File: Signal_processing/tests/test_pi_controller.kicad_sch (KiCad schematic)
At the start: 4 parts, among them X1 Integrator, x1 2nd_Order_Transfer_Function, x2 1st Order Transfer Function

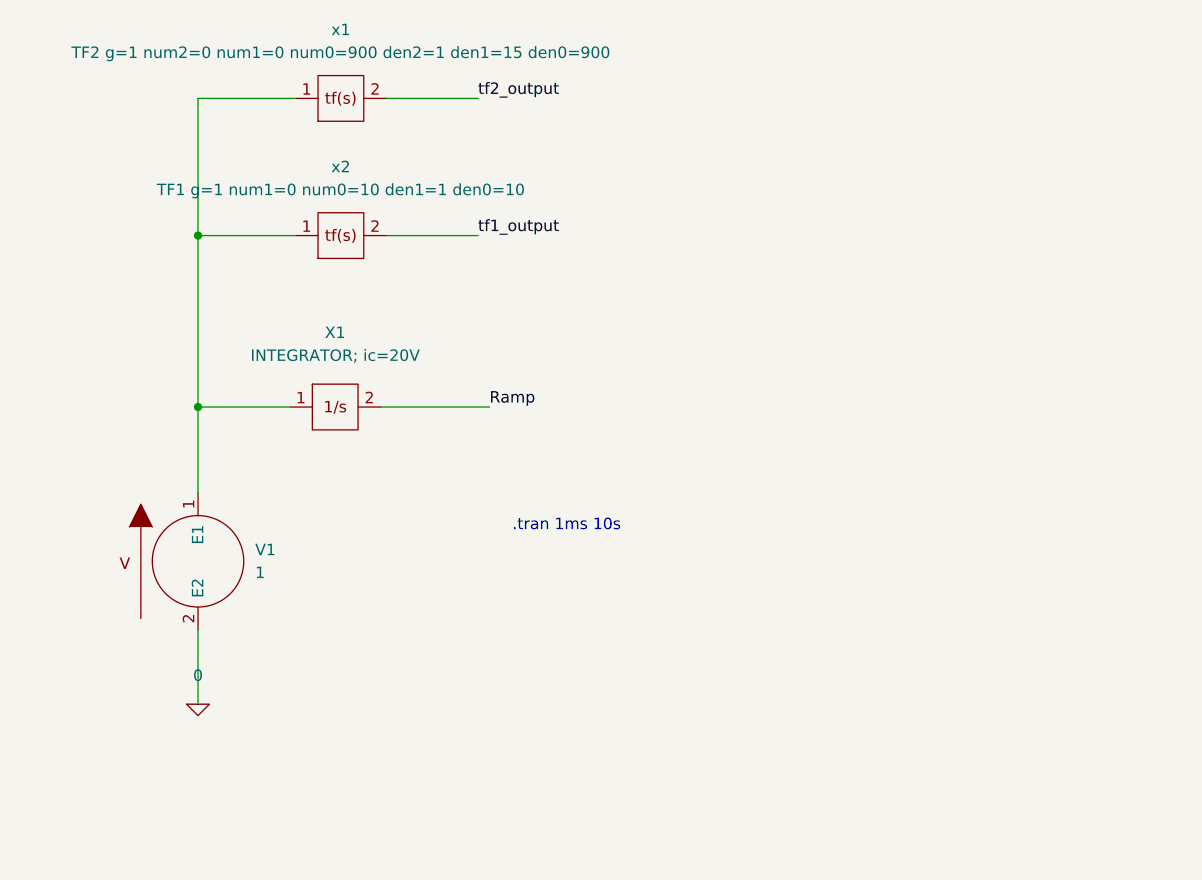
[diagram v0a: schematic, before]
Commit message: Added Sum{2..5}
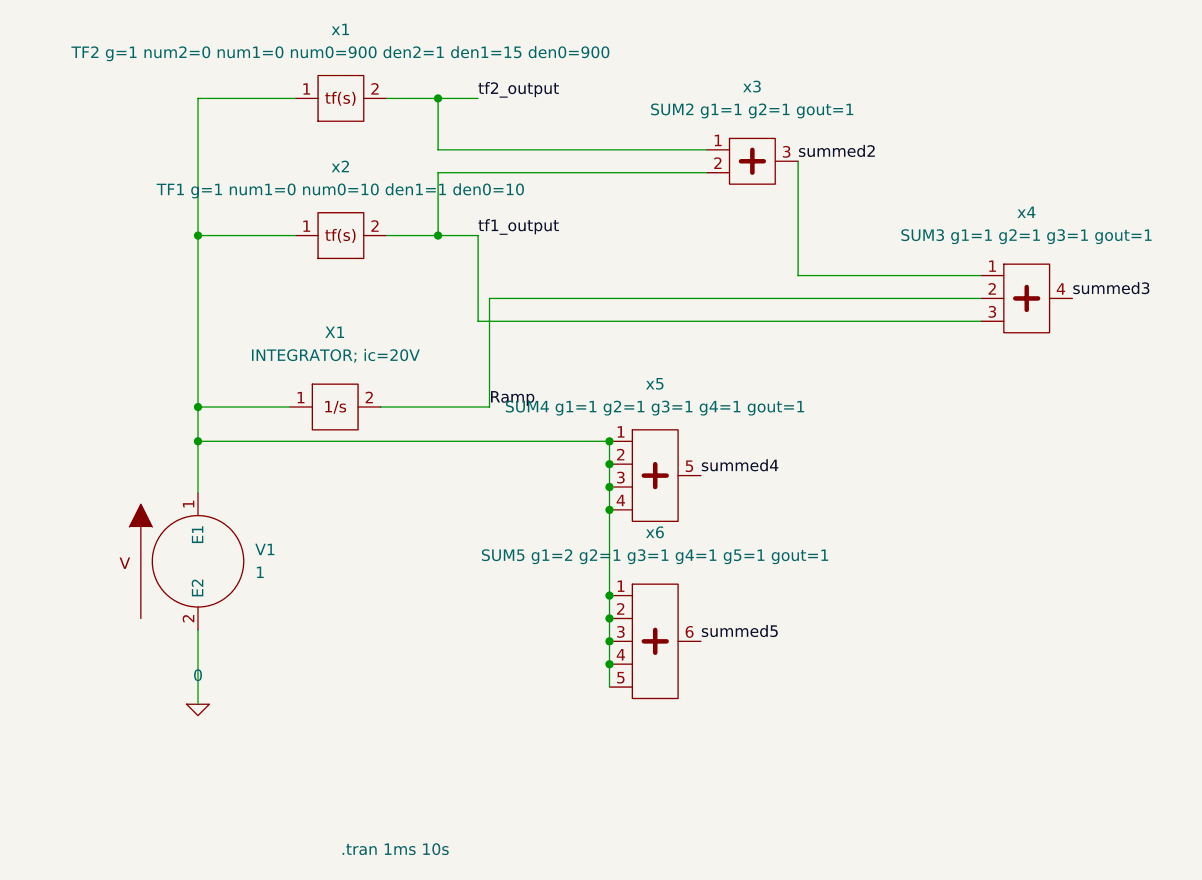
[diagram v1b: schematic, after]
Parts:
- added x3: sum2, symbol Spice_signal_processing:sum2
- added x4: sum3, symbol Spice_signal_processing:sum3
- added x5: sum4, symbol Spice_signal_processing:sum4
- added x6: sum5, symbol Spice_signal_processing:sum5
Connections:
- net Ramp: now also x4.2
- net tf1_output: now also x3.2, x4.3
- net tf2_output: now also x3.1
- net at V1.1 (E1), X1.1, x1.1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: now also x5.1, x5.2, x5.3, x5.4, x6.1, x6.2, x6.3, x6.4, x6.5
- new net summed2: x3.3, x4.1
- new net summed3: x4.4
- new net summed4: x5.5
- new net summed5: x6.6
